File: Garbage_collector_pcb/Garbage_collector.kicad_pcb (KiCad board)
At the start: 2 copper layers, 100 x 100 mm, 111 parts, among them J1 NRF52840, J10 Lidar, J11 VL53L0CXV0DH1, J12 NEOPIXELS, J2 Conn_ST_STDC14, J3 USB_C_Receptacle_PowerOnly_6P, J4 MOTOR2, J5 MOTOR1, J6 SERVO1, J7 SERVO2, J8 VL53L0CXV0DH1, J9 ADA3595, Q1 MMDT2907A-7-F, Q2 DMP1045U-7, Q3 DMN313DLT-7, SW1 SW_Push, SW2 SW_Push, U1 STM32G431RBTx, U2 BQ27220YZFR, U3 BQ25896RTWR, U4 DRV8833PWP, U5 SN74AHCT1G125DBVR, Y1 24MHz

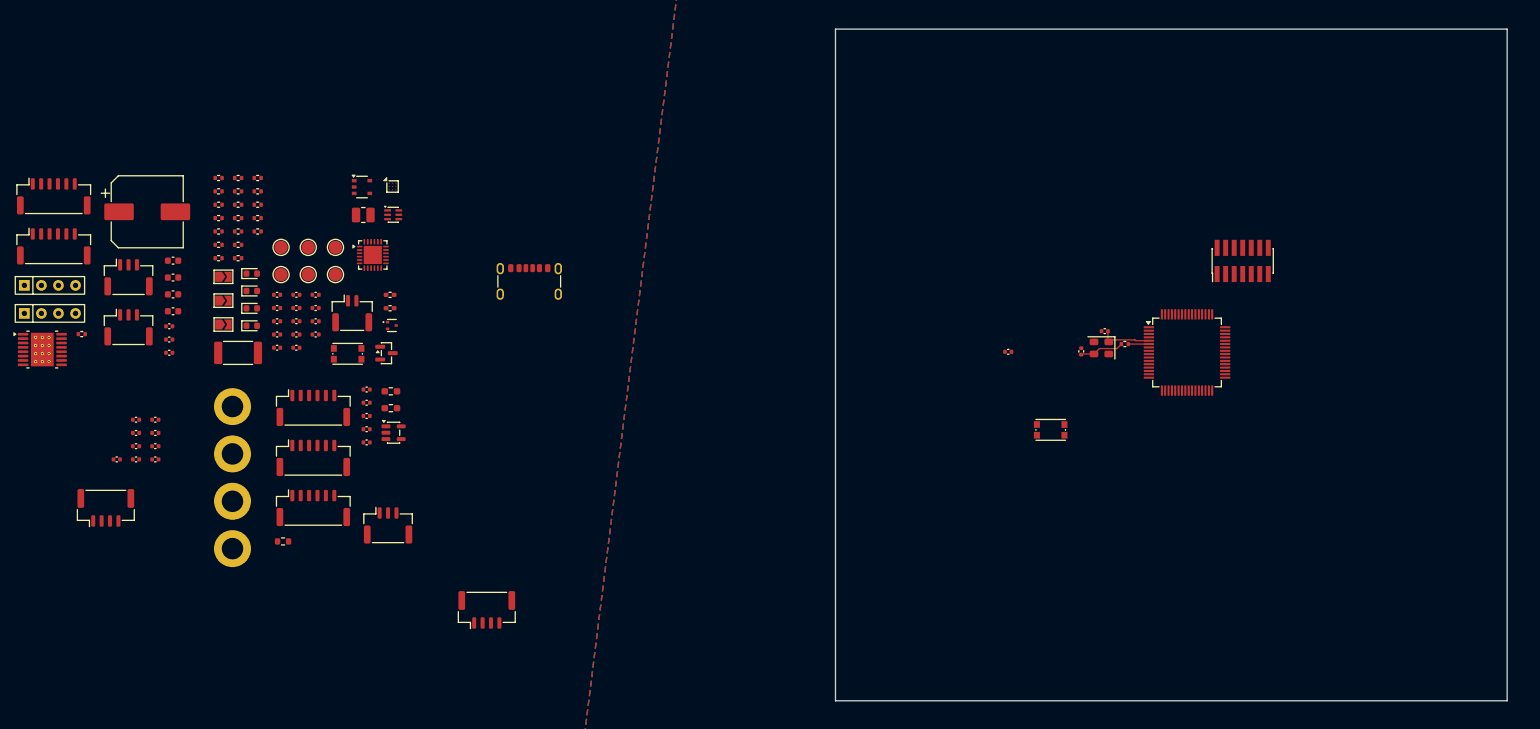
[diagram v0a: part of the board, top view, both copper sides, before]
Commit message: placement des composants pour le routage
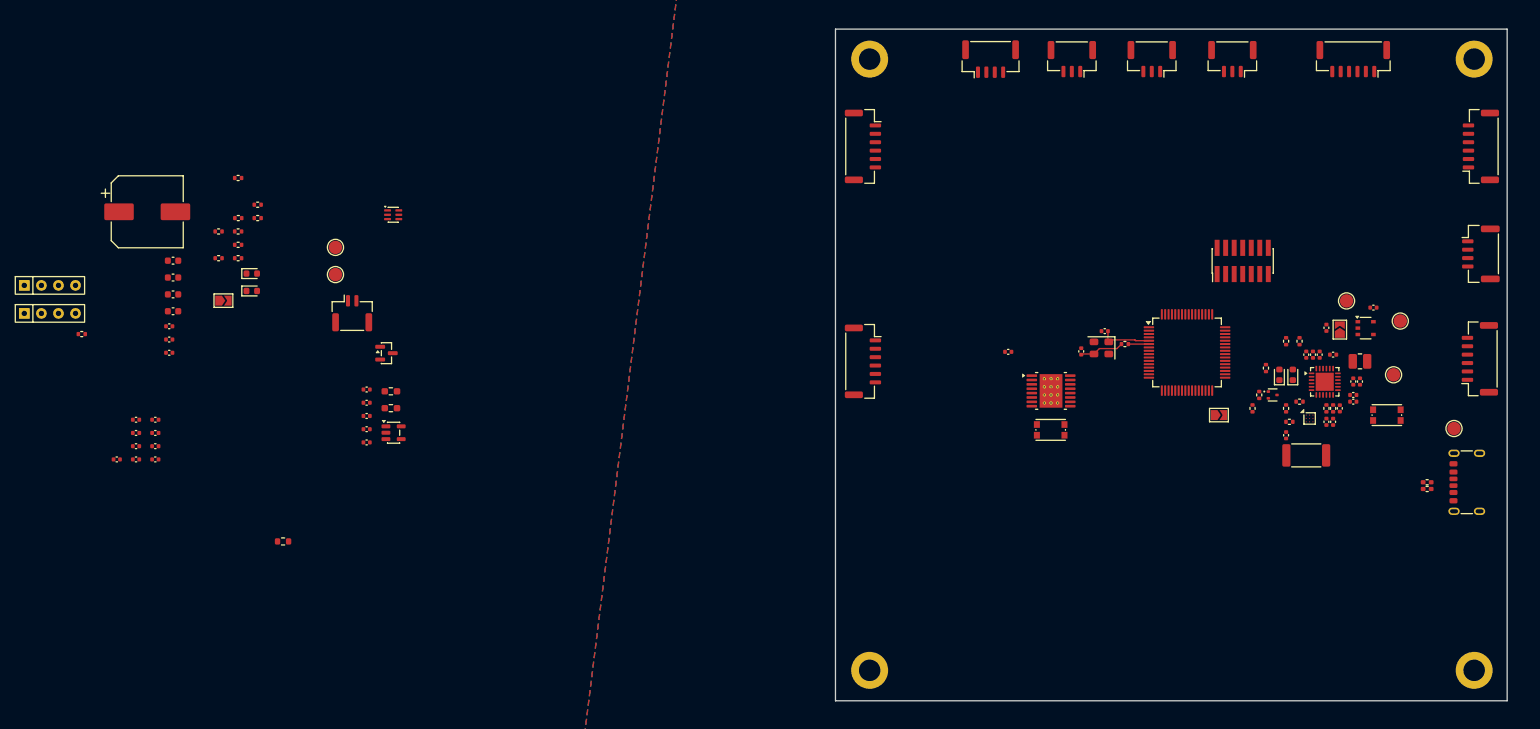
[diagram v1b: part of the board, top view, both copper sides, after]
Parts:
- moved J5 213.0 mm to (234.8, 77.6), turned to 90 degrees
- moved J1 208.2 mm to (235.0, 62.0), turned to -90 degrees
- moved H1 192.0 mm to (234.0, 33.0)
- moved H3 186.6 mm to (234.0, 124.0)
- moved J11 182.0 mm to (235.0, 46.0), turned to 90 degrees
- moved TP2 176.1 mm to (231.0, 88.0)
- moved J7 169.1 mm to (198.0, 33.0), turned to 180 degrees
- moved R8 168.3 mm to (213.0, 85.0), turned to 90 degrees
- moved R10 166.7 mm to (212.0, 85.0), turned to 90 degrees
- moved JP3 166.2 mm to (214.0, 73.3), turned to 90 degrees
- moved J9 165.8 mm to (216.0, 33.0), turned to 180 degrees
- moved R7 163.6 mm to (208.0, 84.0), turned to 180 degrees
- moved C16 163.3 mm to (219.0, 70.0)
- moved R5 163.1 mm to (206.5, 87.0)
- moved TP3 162.9 mm to (223.0, 72.0)
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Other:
- copper layers 2 -> 4

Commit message: placement des composants + routage du pcb
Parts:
- R24, R25: footprint Resistor_THT:R_Array_SIP4 -> Resistor_SMD:R_2512_6332Metric
- moved R12 172.5 mm to (222.0, 63.0), turned to 90 degrees
- moved D1 170.0 mm to (222.0, 66.0), turned to 90 degrees
- moved C8 164.5 mm to (198.0, 72.0)
- moved C11 161.5 mm to (198.0, 71.0)
- moved C7 161.4 mm to (196.0, 83.0), turned to -90 degrees
- moved C4 160.2 mm to (192.0, 85.5), turned to 90 degrees
- moved C12 159.6 mm to (197.0, 83.0), turned to -90 degrees
- moved C37 159.4 mm to (227.1, 64.8), turned to -90 degrees
- moved TP6 157.3 mm to (221.0, 81.0)
- moved C5 157.2 mm to (192.0, 84.0)
- moved C10 155.4 mm to (193.0, 86.0), turned to -90 degrees
- moved R18 154.1 mm to (203.0, 81.0)
- moved R11 152.2 mm to (196.0, 94.0), turned to -90 degrees
- moved C6 150.4 mm to (185.0, 82.0), turned to -90 degrees
- moved C9 149.3 mm to (186.0, 70.0), turned to 180 degrees
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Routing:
- net /Capteurs et périphériques/I2C1_SDA: track 0.00 -> 106.7 mm, vias 0 -> 6
- net /Capteurs et périphériques/I2C1_SCL: track 0.00 -> 99.1 mm, vias 0 -> 15
- net /STM32/NRST: track 0.00 -> 81.8 mm, vias 0 -> 2
- net /Capteurs et périphériques/TOF1_XST: track 0.00 -> 77.0 mm, vias 0 -> 3
- net Net-(J12-Pin_2): track 0.00 -> 68.2 mm, vias 0 -> 2
- net +3.3V: track 0.00 -> 64.8 mm, vias 0 -> 23
- net /Capteurs et périphériques/TOF1_INT: track 0.00 -> 58.4 mm, vias 0 -> 2
- net /STM32/VCP_RX: track 0.00 -> 56.0 mm, vias 0 -> 4
- net /Capteurs et périphériques/Lidar_M_CTRL: track 0.00 -> 53.4 mm, vias 0 -> 2
- net /STM32/VCP_TX: track 0.00 -> 49.8 mm, vias 0 -> 4
- net /Alim/CHARGEUR_QON: track 0.00 -> 44.9 mm, vias 0 -> 2
- net /Capteurs et périphériques/COLOR_INT: track 0.00 -> 44.9 mm, vias 0 -> 4
- net /Capteurs et périphériques/Lidar_TX: track 0.00 -> 42.8 mm, vias 0 -> 2
- net /Moteurs/M2_ENCA: track 0.00 -> 40.8 mm, vias 0 -> 2
- net /Moteurs/M2_ENCB: track 0.00 -> 40.6 mm, vias 0 -> 2
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- added copper zone on In2.Cu, net +3.3V
- added copper zone on In2.Cu, net +5V
- added copper zone on In1.Cu, net GND
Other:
- board size 100 x 100 mm -> 86.9 x 52.9 mm

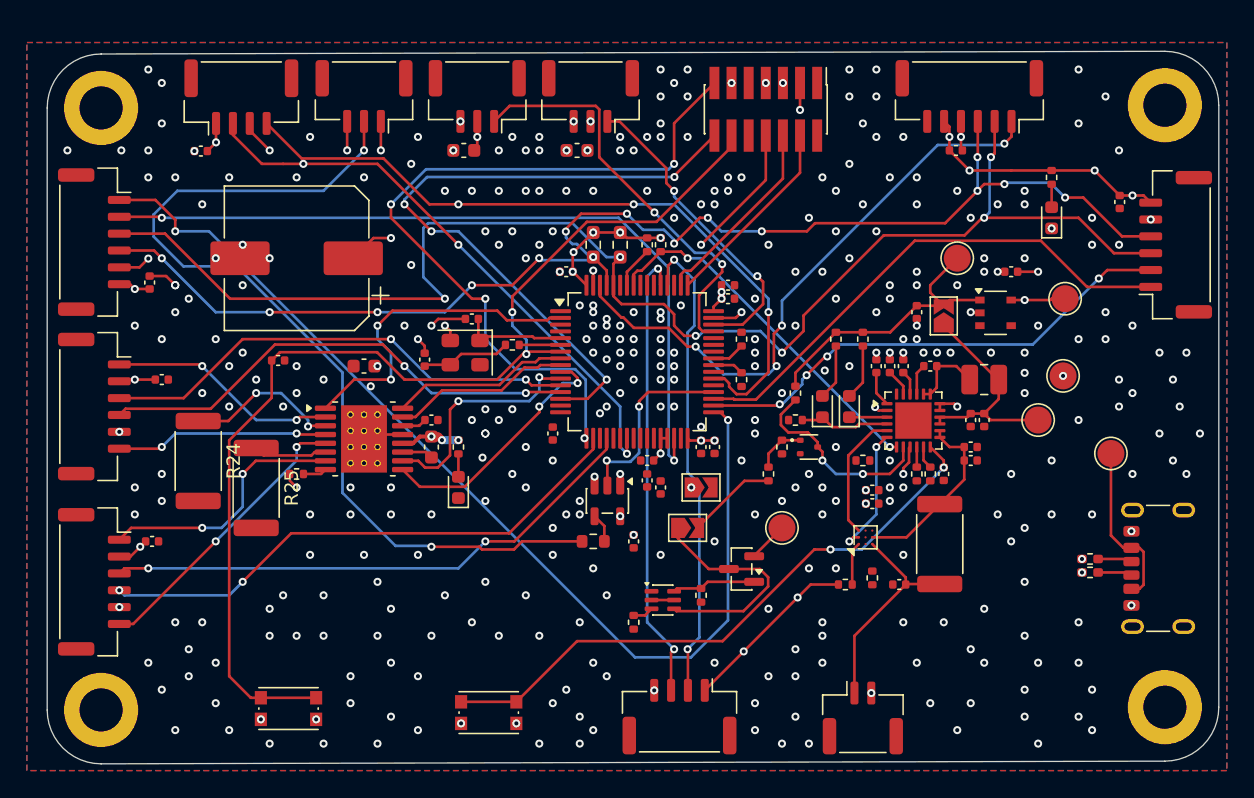
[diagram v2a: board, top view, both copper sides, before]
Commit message: routage du pcb quasiment terminé, 1 erreur DRC
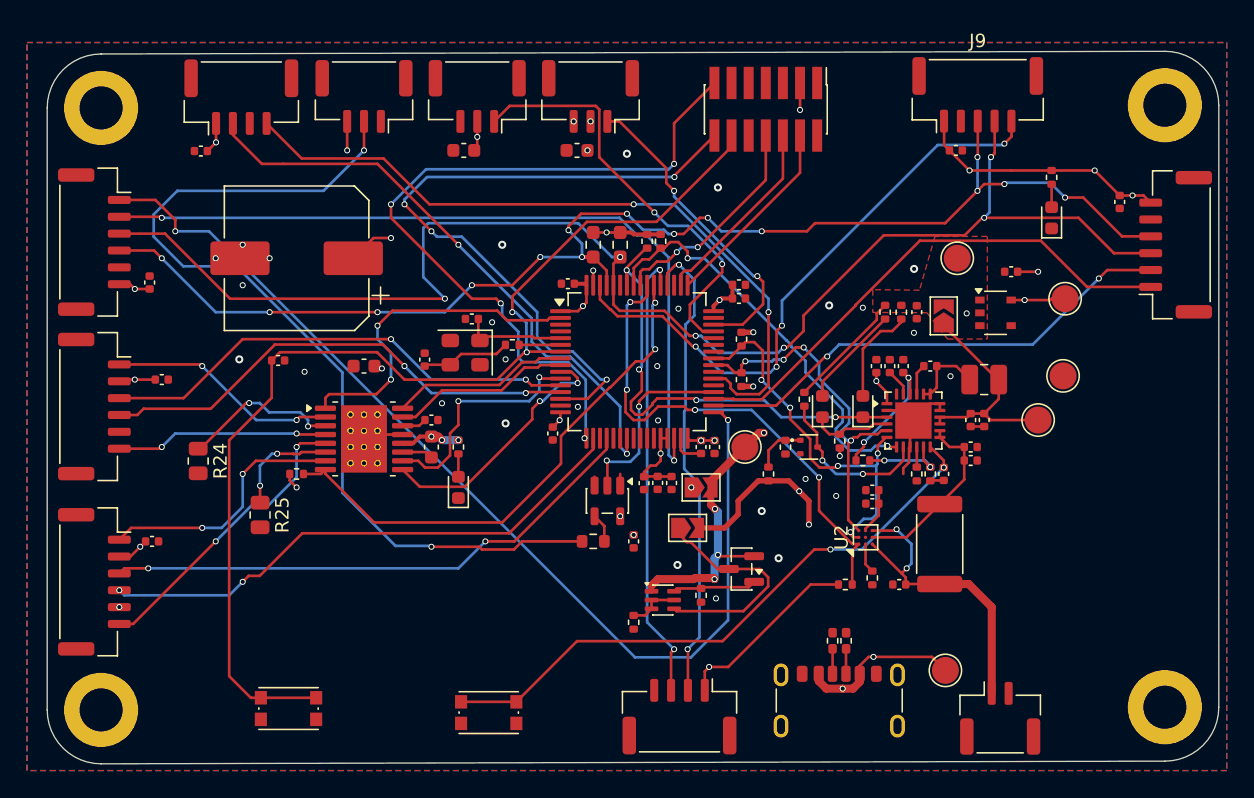
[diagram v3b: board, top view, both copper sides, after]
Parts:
- J9: footprint Connector_JST:JST_GH_SM06B-GHS-TB_1x06-1MP_P1.25mm_Horizontal -> Connector_JST:JST_GH_BM05B-GHS-TBT_1x05-1MP_P1.25mm_Vertical
- R24, R25: footprint Resistor_SMD:R_2512_6332Metric -> Resistor_SMD:R_0805_2012Metric
- U2: footprint Package_BGA:Texas_DSBGA-9_1.4715x1.4715mm_Layout3x3_P0.5mm -> Package_BGA:Texas_DSBGA-9_1.62x1.58mm_Layout3x3_P0.5mm
- moved J3 27.0 mm to (206.2, 102.9), turned to 0 degrees
- moved TP2 20.2 mm to (214.1, 99.6)
- moved R4 19.8 mm to (205.8, 97.4), turned to -90 degrees
- moved R3 19.1 mm to (206.8, 97.4), turned to -90 degrees
- moved BT1 10.2 mm to (218.2, 103.1)
- moved TP5 6.60 mm to (199.2, 83.0)
- moved R20 4.16 mm to (209.7, 73.0)
- moved R18 3.64 mm to (206.3, 82.6), turned to 90 degrees
- moved R23 3.48 mm to (210.8, 73.0)
- moved R25 2.02 mm to (163.3, 88.0)
- moved C5 1.70 mm to (191.8, 85.7), turned to 90 degrees
- moved D4 1.00 mm to (208.0, 80.0)
- moved C9 0.90 mm to (186.1, 70.9)
- moved C10 0.87 mm to (193.8, 85.7)
- moved C11 0.81 mm to (198.8, 71.0)
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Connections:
- J9 pad 1: /Capteurs et périphériques/COLOR_INT -> +3.3V
- J9 pad 2: /Capteurs et périphériques/I2C1_SDA -> GND
- J9 pad 4: GND -> /Capteurs et périphériques/I2C1_SDA
- J9 pad 5: +3.3V -> /Capteurs et périphériques/COLOR_INT
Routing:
- net /Moteurs/MOTOR_FAULT: track 1.76 -> 39.5 mm, vias 0 -> 2
- net /Alim/FG_GPIO: track 3.20 -> 37.4 mm, vias 0 -> 4
- net /Alim/CHARGEUR_PG: track 5.90 -> 36.2 mm, vias 0 -> 4
- net /Alim/VBUS_BQ25: track 5.59 -> 23.7 mm, vias 0 -> 5
- net /Alim/I2C3_SDA: track 12.2 -> 28.7 mm, vias 2 -> 5
- net /Alim/I2C3_SCL: track 11.8 -> 27.1 mm, vias 0 -> 4
- net GND: track 32.3 -> 18.9 mm, vias 367 -> 32
- net SYS: track 21.7 -> 8.94 mm
- net +3.3V: track 64.8 -> 73.8 mm, vias 23 -> 21
- net /Alim/REGN: track 1.80 -> 9.56 mm, vias 0 -> 2
- net /Alim/bat: track 16.2 -> 23.4 mm, vias 0 -> 2
- net /STM32/JTDO/SWO: track 10.1 -> 16.4 mm, vias 1 -> 2
- net VBUS: track 19.2 -> 24.9 mm, vias 0 -> 4
- net Net-(U3-TS): track 1.70 -> 6.45 mm, vias 0 -> 2
- net /Alim/CHARGEUR_INT: track 27.0 -> 30.9 mm
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- added copper zone on In2.Cu, net /Alim/VBUS_BQ25
- added copper zone on F.Cu, net SYS
- added copper zone on In2.Cu, net VBUS

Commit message: fin du routage
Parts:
- removed R17: 10k, Resistor_SMD:R_0402_1005Metric
- C2, C3: value 20pF -> 10pF
- Y1: value 24MHz -> 16MHz
- moved D1 4.47 mm to (224.4, 62.2), turned to -90 degrees
- moved R12 3.97 mm to (225.9, 62.5)
- moved C16 2.10 mm to (220.3, 71.6), turned to -90 degrees
- moved C34 0.95 mm to (186.9, 62.0)
- moved R22 0.41 mm to (199.3, 75.2)
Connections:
- D4 pad 1: /Alim/CHARGEUR_PG -> /Alim/Chargeur_PG
- Q3 pad 3: /Alim/OTG -> /Alim/Chargeur_OTG
- R19 pad 1: /Alim/OTG -> /Alim/Chargeur_OTG
- U1 pad 58: /Alim/CHARGEUR_PG -> /Alim/Chargeur_OTG
- U1 pad 59: /STM32/CHARGEUR_QON -> /Alim/CHARGEUR_QON
- U3 pad 3: /Alim/CHARGEUR_PG -> /Alim/Chargeur_PG
- U3 pad 8: /Alim/OTG -> /Alim/Chargeur_OTG
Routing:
- net /Alim/CHARGEUR_PG: track 36.2 -> 0.00 mm, vias 4 -> 0
- net /Alim/Chargeur_OTG: track 0.00 -> 31.8 mm, vias 0 -> 6
- net /Alim/CHARGEUR_QON: track 44.9 -> 75.5 mm, vias 2 -> 6
- net +3.3V: track 73.8 -> 59.7 mm, vias 21 -> 20
- net /Alim/OTG: track 12.4 -> 0.00 mm, vias 2 -> 0
- net +5V: track 15.2 -> 20.4 mm, vias 13 -> 10
- net /Alim/Chargeur_PG: track 0.00 -> 1.79 mm
- net +BATT: track 13.6 -> 15.2 mm
- net /Alim/I2C3_SDA: track 28.7 -> 27.9 mm
- net Net-(U3-TS): track 6.45 -> 5.69 mm
- net /Alim/CHARGEUR_INT: track 30.9 -> 30.2 mm
- net /Capteurs et périphériques/TOF2_XST: track 38.8 -> 39.4 mm
- net /Capteurs et périphériques/I2C1_SCL: track 97.5 -> 97.1 mm, vias 15 -> 12
- net Net-(U4-BISEN): track 8.04 -> 8.19 mm, vias 2 -> 0
- net GND: vias 32 -> 129
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
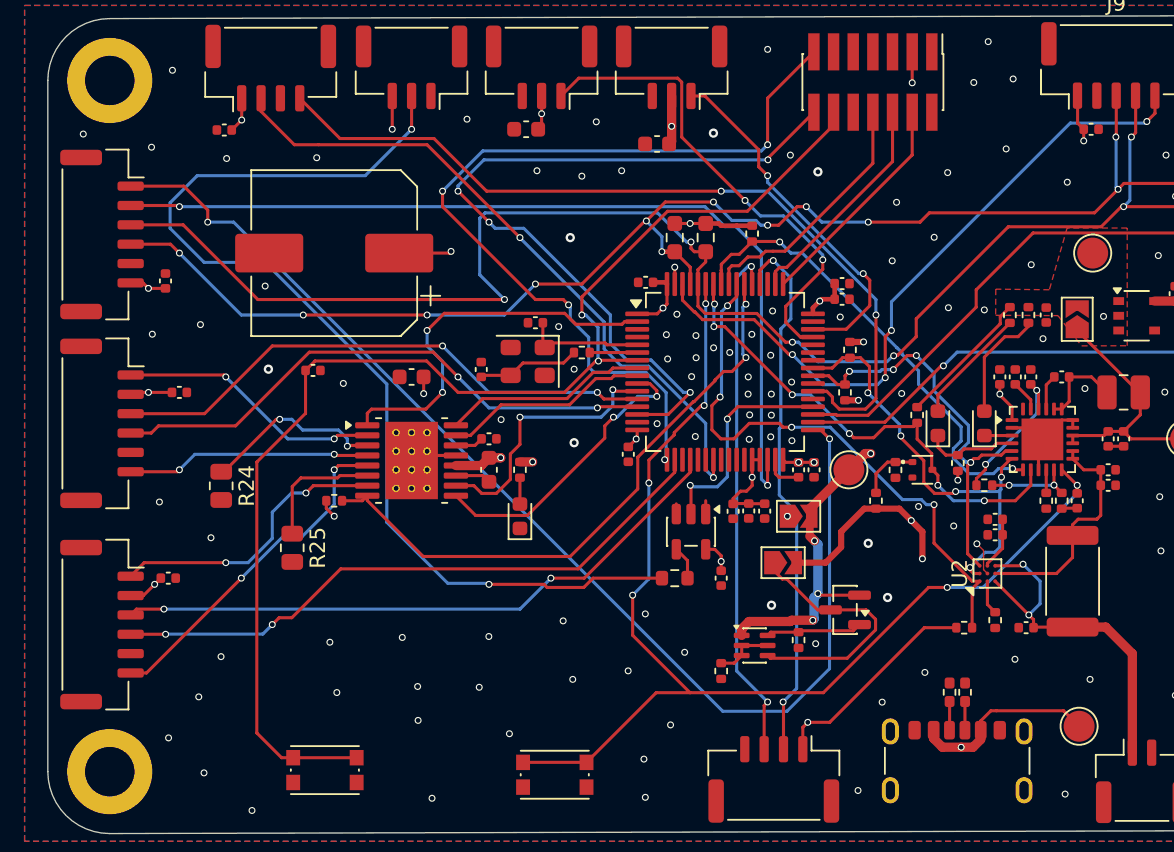
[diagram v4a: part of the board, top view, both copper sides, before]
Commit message: ajout de zones pour Aout1, Aout2, Bout1, Bout2 (moteurs)
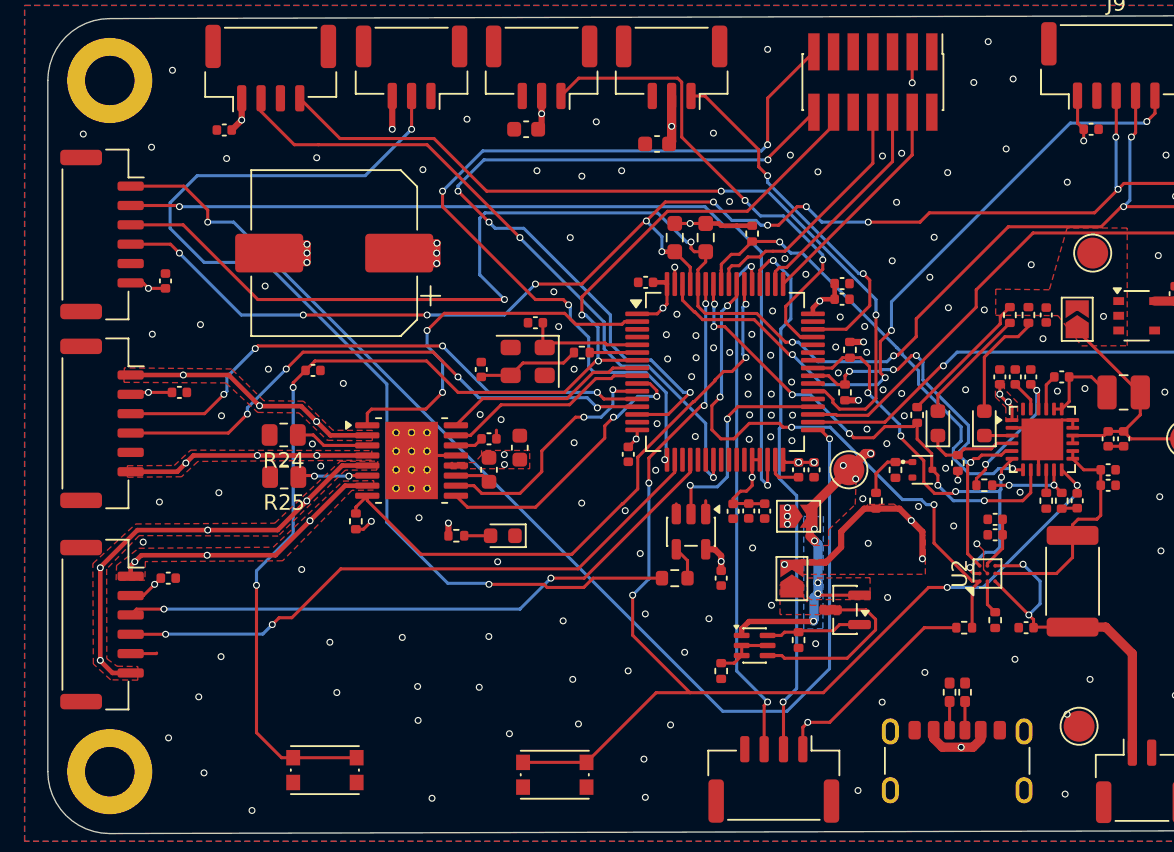
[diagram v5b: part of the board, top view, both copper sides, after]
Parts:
- moved C28 8.35 mm to (178.0, 81.6), turned to 90 degrees
- moved R15 5.92 mm to (173.9, 87.3), turned to 180 degrees
- moved R24 5.21 mm to (162.7, 80.8), turned to 180 degrees
- moved R25 4.60 mm to (162.8, 83.5), turned to 180 degrees
- moved R26 1.93 mm to (167.4, 86.3), turned to 90 degrees
- moved D2 1.68 mm to (176.9, 87.3), turned to 180 degrees
- moved JP2 1.18 mm to (195.6, 90.0), turned to 90 degrees
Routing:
- net GND: track 18.9 -> 27.7 mm, vias 129 -> 169
- net Net-(U4-AISEN): track 11.9 -> 4.76 mm, vias 2 -> 0
- net VBUS: track 24.9 -> 18.4 mm, vias 3 -> 5
- net /Moteurs/BOUT2: track 22.1 -> 28.3 mm, vias 2 -> 4
- net Net-(JP2-A): track 16.9 -> 11.7 mm
- net Net-(U4-BISEN): track 8.19 -> 4.53 mm, vias 0 -> 2
- net /Moteurs/BIN2: track 17.3 -> 16.1 mm
- net +5V: track 20.4 -> 19.6 mm, vias 10 -> 14
- net /Moteurs/BOUT1: track 18.7 -> 18.1 mm, vias 2 -> 3
- net /Moteurs/M1_ENCA: track 36.0 -> 36.5 mm, vias 2 -> 4
- net /Moteurs/M1_ENCB: track 36.4 -> 36.6 mm, vias 2 -> 4
- net /Moteurs/AOUT1: track 17.1 -> 16.9 mm, vias 2 -> 3
- net /Alim/VBUS_BQ25: vias 5 -> 10
- net /Moteurs/AOUT2: track 15.8 -> 15.7 mm, vias 2 -> 3
- net /STM32/NRST: vias 2 -> 4
- added copper zone on F.Cu, net +5V
- added copper zone on B.Cu, net /Alim/VBUS_BQ25
- added copper zone on F.Cu, net /Alim/VBUS_BQ25
- added copper zone on F.Cu, net /Moteurs/AOUT1
- added copper zone on F.Cu, net /Moteurs/AOUT2
- added copper zone on F.Cu, net /Moteurs/BOUT1
- added copper zone on F.Cu, net /Moteurs/BOUT2
- added copper zone on F.Cu, net Net-(JP2-A)
- added copper zone on F.Cu, net VBUS
